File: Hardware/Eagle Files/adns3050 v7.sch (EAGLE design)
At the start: 7 parts, among them U1 V_REG_317SMD

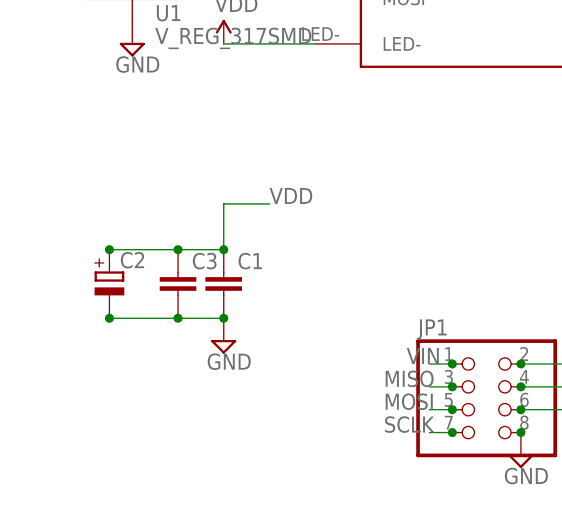
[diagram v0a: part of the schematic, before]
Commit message: Updated board, increased text spacing
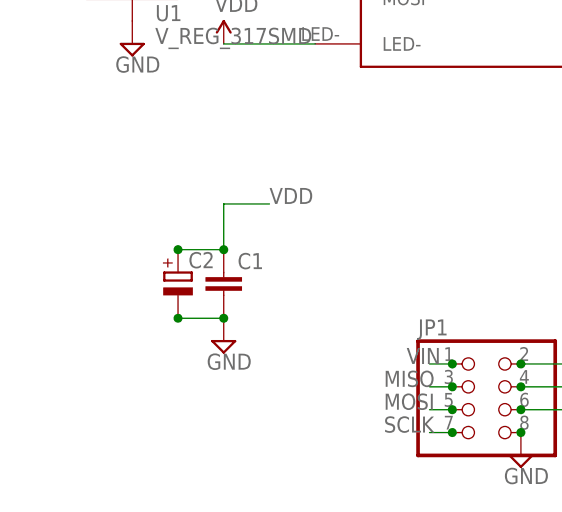
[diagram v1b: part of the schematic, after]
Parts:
- removed C3: (no value), eagle-ltspice:CC0603
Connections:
- net GND: no longer C3.2
- net VDD: no longer C3.1
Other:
- moved on the sheet: C2
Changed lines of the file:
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@@
 <part name="JP1" library="pinhead" deviceset="PINHD-2X4" device=""/>
 <part name="C2" library="rcl" deviceset="CPOL-EU" device="R/2012-12R"/>
-<part name="C3" library="eagle-ltspice" deviceset="C" device="C0603"/>
 </parts>
 <sheets>
@@
 <instance part="SUPPLY7" gate="GND" x="66.04" y="139.7"/>
 <instance part="JP1" gate="A" x="104.14" y="99.06"/>
-<instance part="C2" gate="G$1" x="63.5" y="114.3"/>
-<instance part="C3" gate="G$1" x="71.12" y="114.3"/>
+<instance part="C2" gate="G$1" x="71.12" y="114.3"/>
 </instances>
 <busses>
@@
 <label x="81.28" y="121.92" size="1.778" layer="95"/>
 <pinref part="C2" gate="G$1" pin="+"/>
+<junction x="71.12" y="116.84"/>
 <wire x1="76.2" y1="116.84" x2="71.12" y2="116.84" width="0.1524" layer="91"/>
-<junction x="63.5" y="116.84"/>
-<pinref part="C3" gate="G$1" pin="1"/>
-<junction x="71.12" y="116.84"/>
-<wire x1="71.12" y1="116.84" x2="63.5" y2="116.84" width="0.1524" layer="91"/>
 <junction x="76.2" y="116.84"/>
 </segment>
@@
 <pinref part="SUPPLY5" gate="GND" pin="GND"/>
 <pinref part="C2" gate="G$1" pin="-"/>
-<wire x1="63.5" y1="109.22" x2="71.12" y2="109.22" width="0.1524" layer="91"/>
+<wire x1="71.12" y1="109.22" x2="76.2" y2="109.22" width="0.1524" layer="91"/>
 <junction x="76.2" y="109.22"/>
-<pinref part="C3" gate="G$1" pin="2"/>
 <junction x="71.12" y="109.22"/>
-<wire x1="71.12" y1="109.22" x2="76.2" y2="109.22" width="0.1524" layer="91"/>
-<junction x="63.5" y="109.22"/>
 </segment>
 <segment>
